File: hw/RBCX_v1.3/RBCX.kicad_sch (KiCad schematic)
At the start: 10 parts, among them J1 Conn_02x02_Odd_Even

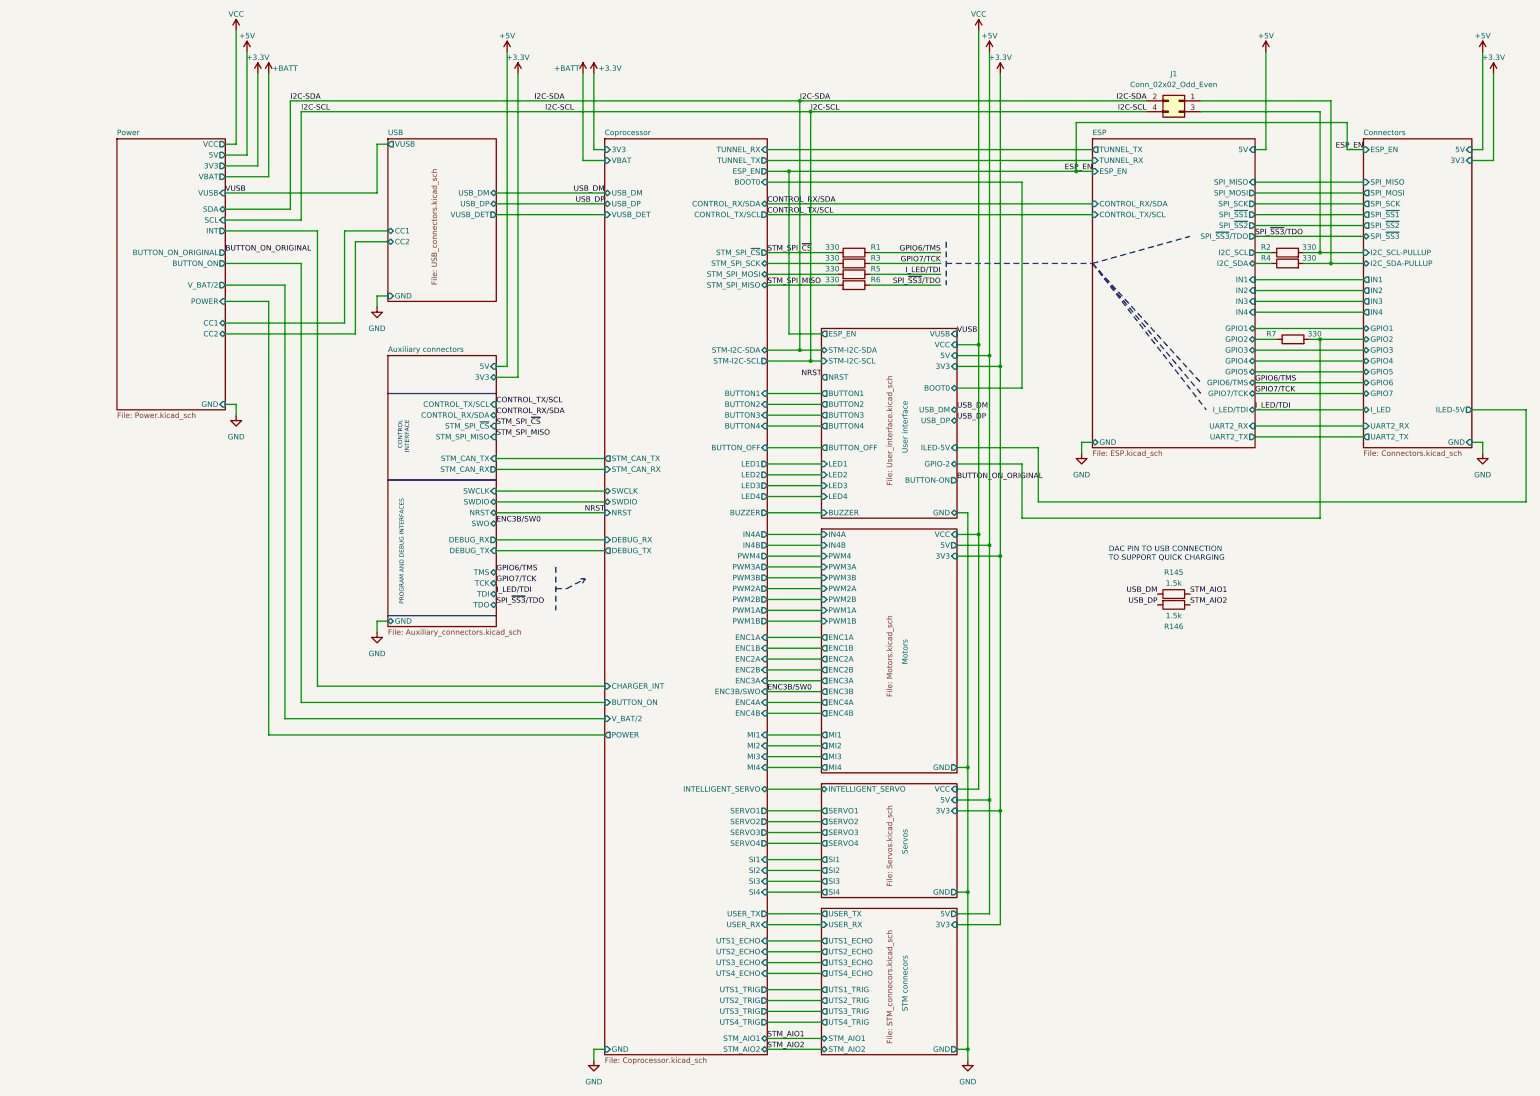
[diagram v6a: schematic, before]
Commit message: Protective resistors for I2C on connectors
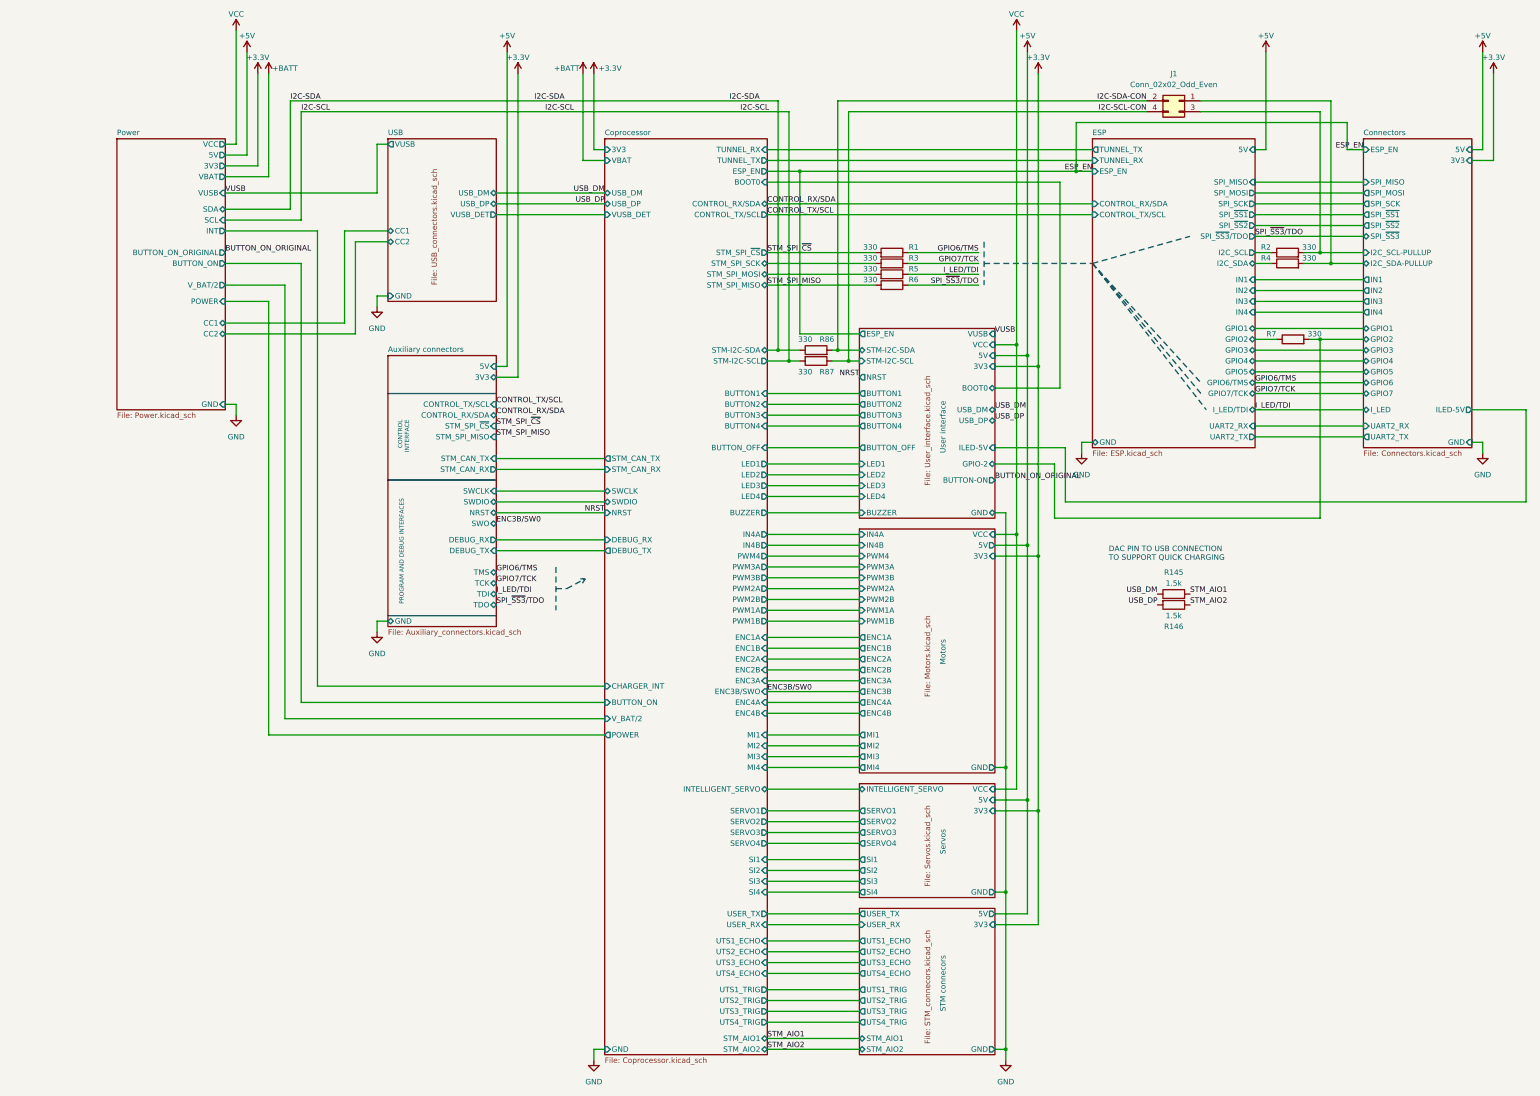
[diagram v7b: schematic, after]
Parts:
- added R86, R87: 330, Capacitor_SMD:C_0201_0603Metric, symbol Device:R
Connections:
- net I2C-SCL: now also R87.2; no longer J1.4 (Pin_4)
- net I2C-SDA: now also R86.1; no longer J1.2 (Pin_2)
- new net I2C-SCL-CON: J1.4 (Pin_4), R87.1
- new net I2C-SDA-CON: J1.2 (Pin_2), R86.2
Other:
- moved on the sheet: R1, R3, R5, R6

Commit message: Kuba issues
Change of power transistor from JSM3622 to JMSL0302AU

NTC connectors

Moving the Cell balancer behind the switch

and some little things
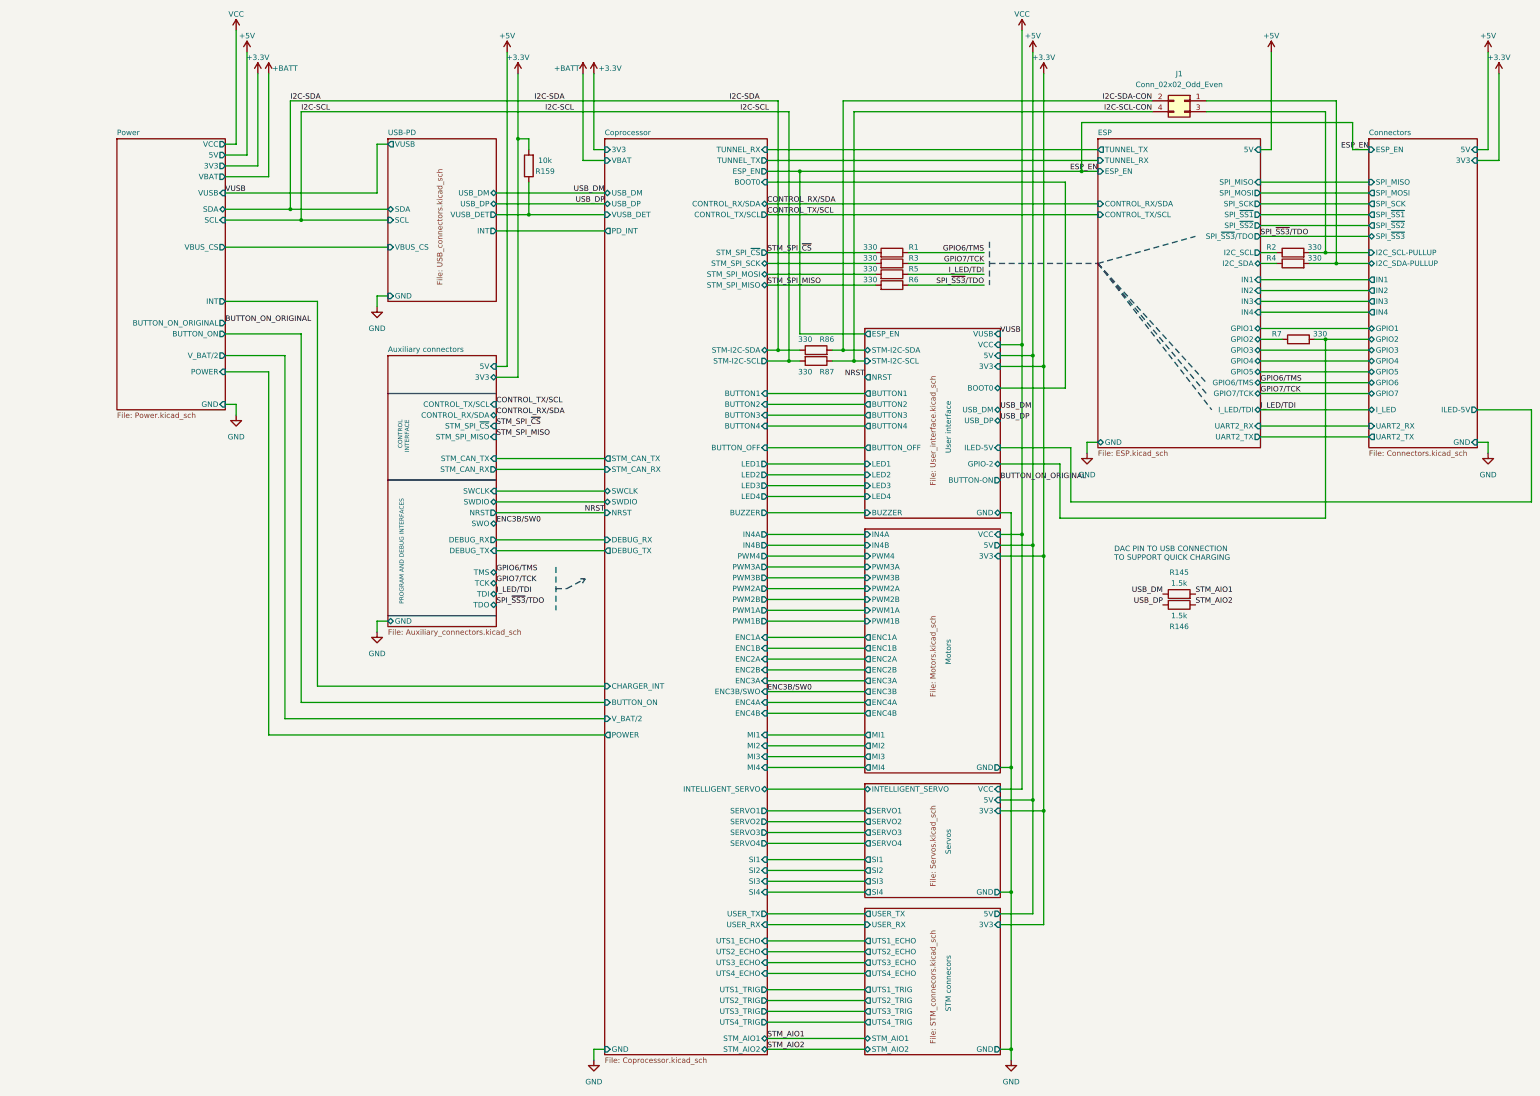
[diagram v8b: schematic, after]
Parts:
- added R159: 10k, Capacitor_SMD:C_0201_0603Metric, symbol Device:R
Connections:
- net +3.3V: now also R159.2
- net Coprocessor/VUSB_DET: now also R159.1
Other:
- sheet USB renamed USB-PD
- sheet Coprocessor ports: added PD_INT; removed none
- sheet Power ports: added VBUS_CS; removed CC1, CC2
- sheet USB-PD ports: added INT, SCL, SDA, VBUS_CS; removed CC1, CC2
- moved on the sheet: J1, R145, R146, R2, R4, R7
